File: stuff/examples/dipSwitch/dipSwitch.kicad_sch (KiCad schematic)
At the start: 6 parts, among them SW1 SWITCH, SW2 SW_DIP_x01

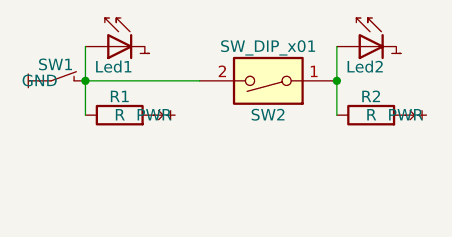
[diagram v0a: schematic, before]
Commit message: DimSwitch filter fix with multiple DIP on one NET
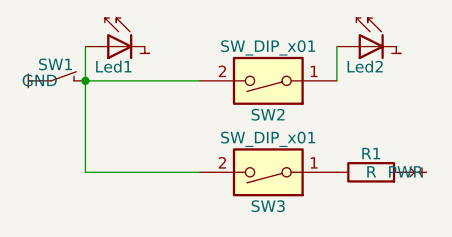
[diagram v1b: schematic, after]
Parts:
- removed R2: R, symbol Device:R
- added SW3: SW_DIP_x01, symbol Switch:SW_DIP_x01
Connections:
- net at Led1.1 (IN), SW1.2 (IN2), SW2.2: now also SW3.2; no longer R1.1
- new net: R1.1, SW3.1
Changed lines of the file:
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@@
 (kicad_sch (version 20230121) (generator eeschema)
   (paper "A4")
-  (junction (at 142.24 71.755) (diameter 0) (color 0 0 0 0)
-  )
   (junction (at 114.3 71.755) (diameter 0) (color 0 0 0 0)
   )
-  (wire (pts (xy 114.3 71.755) (xy 114.3 75.565))
+  (wire (pts (xy 114.3 71.755) (xy 114.3 81.915))
+    (stroke (width 0) (type default))
+  )
+  (wire (pts (xy 114.3 81.915) (xy 127 81.915))
     (stroke (width 0) (type default))
   )
   (wire (pts (xy 114.3 71.755) (xy 127 71.755))
-    (stroke (width 0) (type default))
-  )
-  (wire (pts (xy 142.24 71.755) (xy 142.24 75.565))
     (stroke (width 0) (type default))
   )
@@
     (stroke (width 0) (type default))
   )
-  (symbol (lib_id "Device:R") (at 146.05 75.565 90) (unit 1)
-    (in_bom yes) (on_board yes) (dnp no)
-    (property "Reference" "R2" (at 146.05 73.533 90)
-      (effects (font (size 1.27 1.27)))
-    )
-    (property "Value" "R" (at 146.05 75.565 90)
-      (effects (font (size 1.27 1.27)))
-    )
-    (property "Footprint" "" (at 146.05 77.343 90)
+  (symbol (lib_id "chip:PWR") (at 149.86 81.915 180) (unit 1)
+    (in_bom no) (on_board no) (dnp no)
+    (property "Reference" "#PWR01" (at 156.21 80.645 0)
       (effects (font (size 1.27 1.27)) hide)
     )
-    (property "Datasheet" "~" (at 146.05 75.565 0)
+    (property "Value" "PWR" (at 149.86 81.915 0)
+      (effects (font (size 0 0)))
+    )
+    (property "Footprint" "" (at 153.416 79.375 0)
+      (effects (font (size 1.27 1.27)) hide)
+    )
+    (property "Datasheet" "" (at 153.416 79.375 0)
       (effects (font (size 1.27 1.27)) hide)
     )
     (pin "1")
-    (pin "2")
     (instances
       (project "dipSwitch"
         (path "/dca00733-6e59-4b89-b3a6-bb50926963b6"
-          (reference "R2") (unit 1)
+          (reference "#PWR01") (unit 1)
         )
       )
@@
     )
   )
-  (symbol (lib_id "Device:R") (at 118.11 75.565 90) (unit 1)
+  (symbol (lib_id "Switch:SW_DIP_x01") (at 134.62 81.915 180) (unit 1)
     (in_bom yes) (on_board yes) (dnp no)
-    (property "Reference" "R1" (at 118.11 73.533 90)
+    (property "Reference" "SW3" (at 134.62 85.725 0)
       (effects (font (size 1.27 1.27)))
     )
-    (property "Value" "R" (at 118.11 75.565 90)
+    (property "Value" "SW_DIP_x01" (at 134.62 78.105 0)
       (effects (font (size 1.27 1.27)))
     )
-    (property "Footprint" "" (at 118.11 77.343 90)
+    (property "Footprint" "" (at 134.62 81.915 0)
       (effects (font (size 1.27 1.27)) hide)
     )
-    (property "Datasheet" "~" (at 118.11 75.565 0)
+    (property "Datasheet" "~" (at 134.62 81.915 0)
+      (effects (font (size 1.27 1.27)) hide)
+    )
+    (pin "2")
+    (pin "1")
+    (instances
+      (project "dipSwitch"
+        (path "/dca00733-6e59-4b89-b3a6-bb50926963b6"
+          (reference "SW3") (unit 1)
+        )
+      )
+    )
+  )
+  (symbol (lib_id "Device:R") (at 146.05 81.915 90) (unit 1)
+    (in_bom yes) (on_board yes) (dnp no)
+    (property "Reference" "R1" (at 146.05 79.883 90)
+      (effects (font (size 1.27 1.27)))
+    )
+    (property "Value" "R" (at 146.05 81.915 90)
+      (effects (font (size 1.27 1.27)))
+    )
+    (property "Footprint" "" (at 146.05 83.693 90)
+      (effects (font (size 1.27 1.27)) hide)
+    )
+    (property "Datasheet" "~" (at 146.05 81.915 0)
       (effects (font (size 1.27 1.27)) hide)
     )
@@
     )
   )
-  (symbol (lib_id "chip:PWR") (at 121.92 75.565 180) (unit 1)
-    (in_bom no) (on_board no) (dnp no)
-    (property "Reference" "#PWR01" (at 128.27 74.295 0)
-      (effects (font (size 1.27 1.27)) hide)
-    )
-    (property "Value" "PWR" (at 121.92 75.565 0)
-      (effects (font (size 0 0)))
-    )
-    (property "Footprint" "" (at 125.476 73.025 0)
-      (effects (font (size 1.27 1.27)) hide)
-    )
-    (property "Datasheet" "" (at 125.476 73.025 0)
-      (effects (font (size 1.27 1.27)) hide)
-    )
-    (pin "1")
-    (instances
-      (project "dipSwitch"
-        (path "/dca00733-6e59-4b89-b3a6-bb50926963b6"
-          (reference "#PWR01") (unit 1)
-        )
-      )
-    )
-  )
   (symbol (lib_id "chip:LED") (at 114.3 67.945 0) (unit 1)
     (in_bom yes) (on_board yes) (dnp no)
@@
         )
       )
-    )
-  )
-  (symbol (lib_id "chip:PWR") (at 149.86 75.565 180) (unit 1)
-    (in_bom no) (on_board no) (dnp no)
-    (property "Reference" "#PWR02" (at 156.21 74.295 0)
-      (effects (font (size 1.27 1.27)) hide)
-    )
-    (property "Value" "PWR" (at 149.86 75.565 0)
-      (effects (font (size 0 0)))
-    )
-    (property "Footprint" "" (at 153.416 73.025 0)
-      (effects (font (size 1.27 1.27)) hide)
-    )
-    (property "Datasheet" "" (at 153.416 73.025 0)
-      (effects (font (size 1.27 1.27)) hide)
-    )
-    (pin "1")
-    (instances
-      (project "dipSwitch"
-        (path "/dca00733-6e59-4b89-b3a6-bb50926963b6"
-          (reference "#PWR02") (unit 1)
-        )
-      )
